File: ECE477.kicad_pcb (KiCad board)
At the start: 2 copper layers, 58 parts, among them IC1 LP3852EMP-3.3_NOPB, IC2 BQ29330DBT, J1 P7805-2000-S, J2 Conn_01x05_Male, J3 Conn_01x05_Male, J4 Conn_01x05_Male, J5 Conn_01x05_Male, J6 Conn_01x05_Male, J7 Conn_01x05_Male, SW1 SW_Push_Dual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

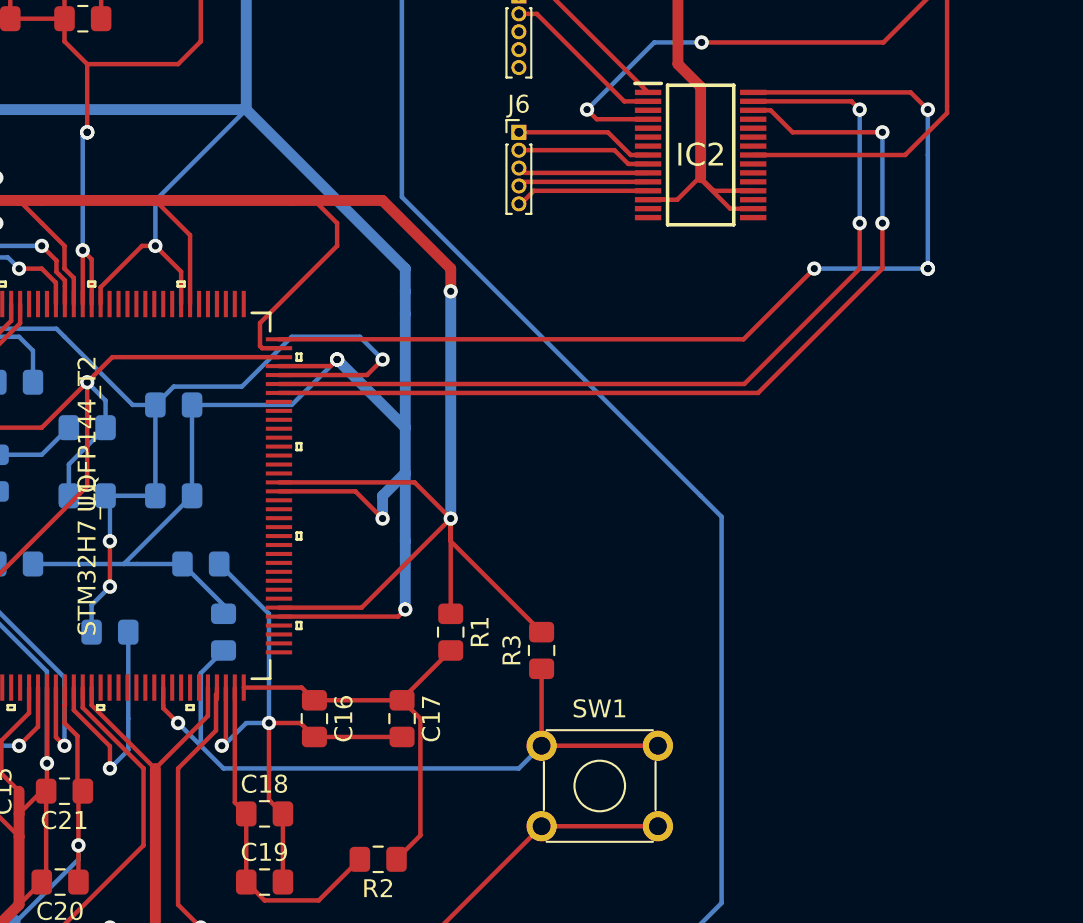
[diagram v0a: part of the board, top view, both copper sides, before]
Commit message: Updated CLK for Bq29330DBT
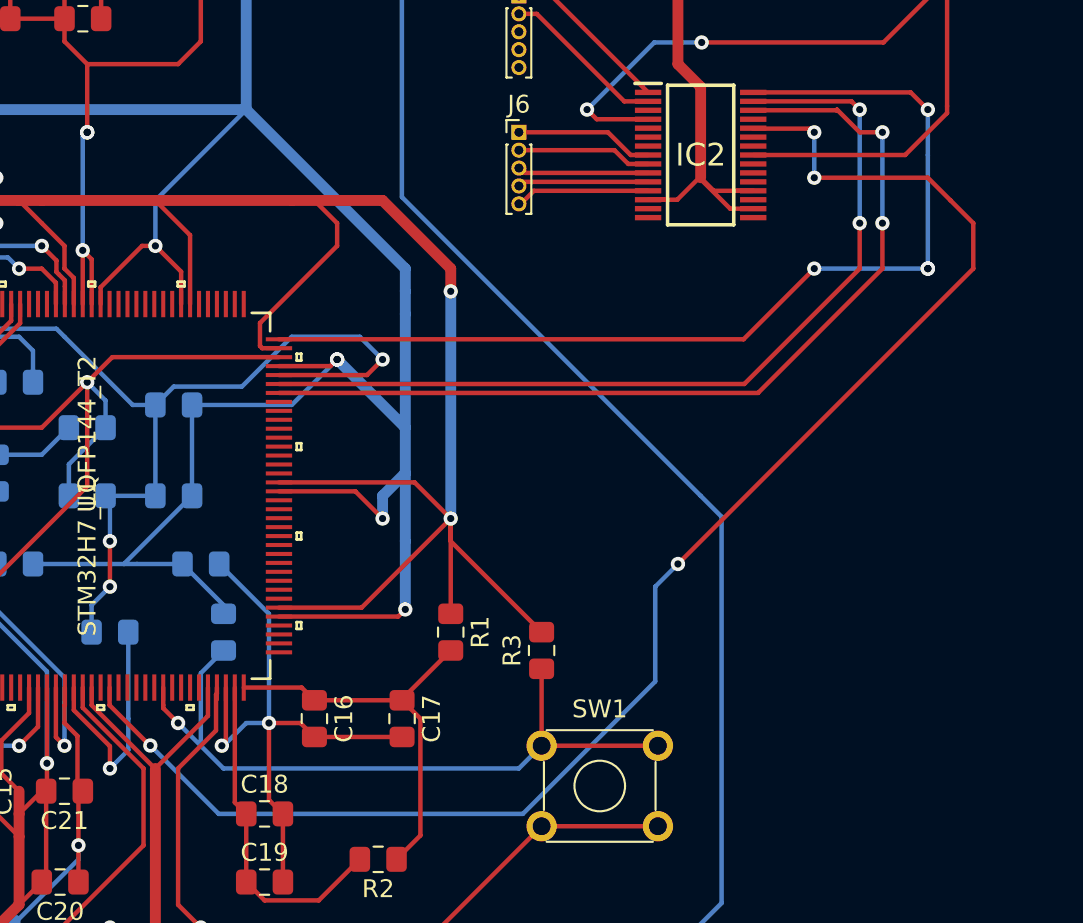
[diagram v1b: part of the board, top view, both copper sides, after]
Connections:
- IC2 pad 26: Net-(IC2-Pad26) -> CLK
- U1 pad 21: Net-(U1-Pad21) -> CLK
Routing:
- net CLK: track 0.00 -> 86.1 mm, vias 0 -> 4

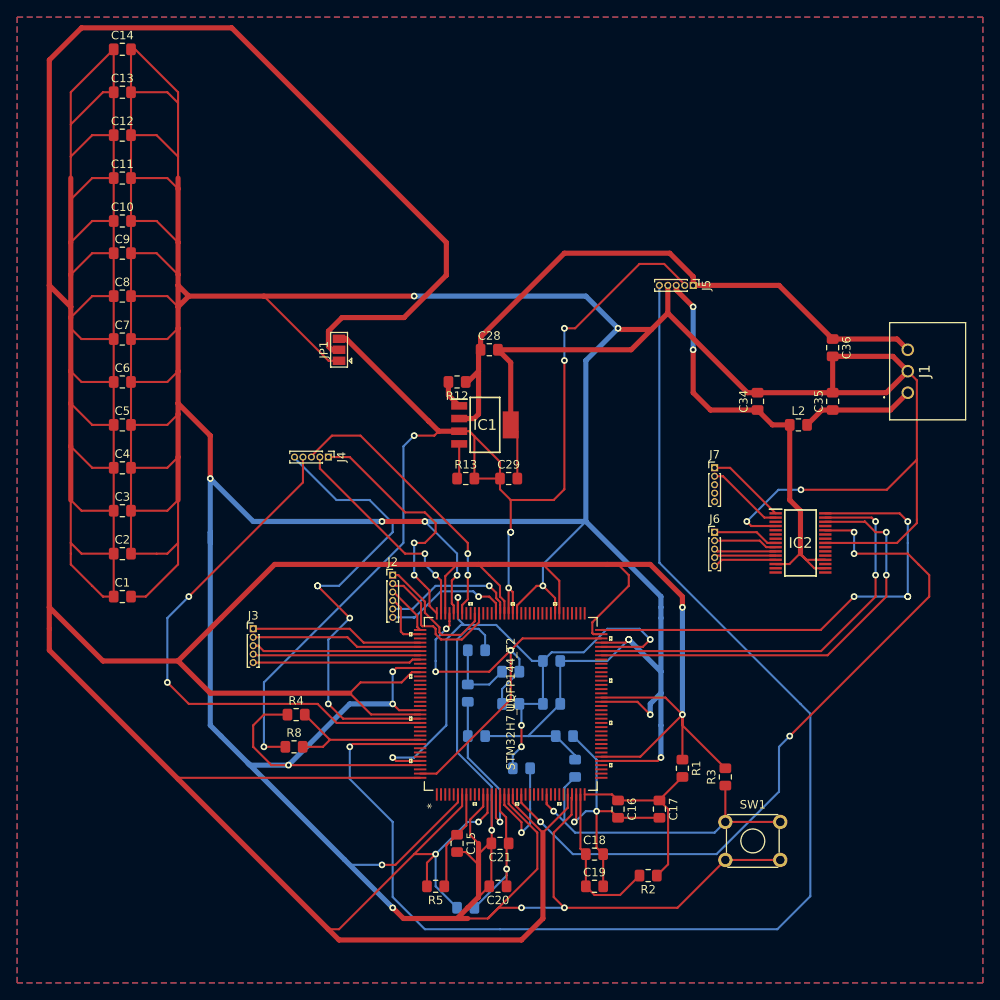
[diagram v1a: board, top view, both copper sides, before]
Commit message: Added mounting Holes
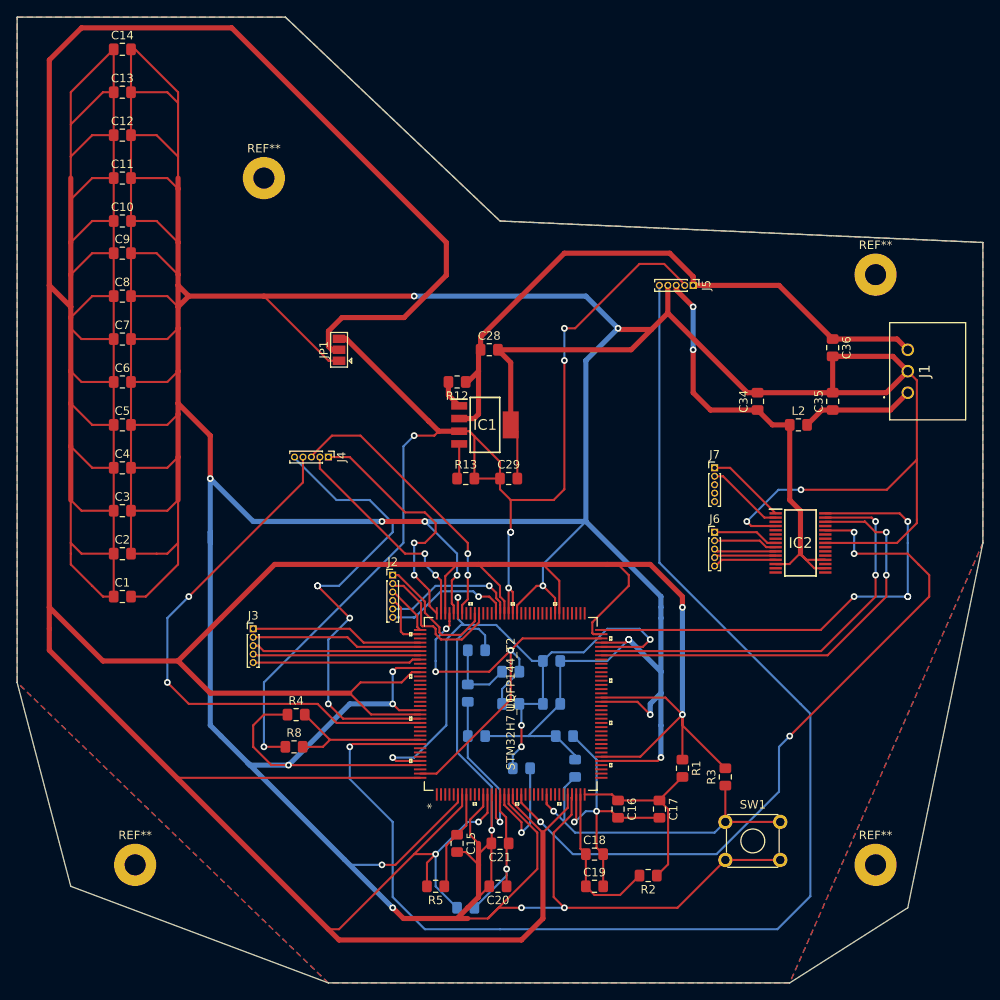
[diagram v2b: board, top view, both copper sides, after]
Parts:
- added REF**: MountingHole_2.5mm_Pad, MountingHole:MountingHole_2.5mm_Pad, F.Cu at (168.9, 44.5)
- added REF**: MountingHole_2.5mm_Pad, MountingHole:MountingHole_2.5mm_Pad, F.Cu at (241.3, 55.9)
- added REF**: MountingHole_2.5mm_Pad, MountingHole:MountingHole_2.5mm_Pad, F.Cu at (153.7, 125.7)
- added REF**: MountingHole_2.5mm_Pad, MountingHole:MountingHole_2.5mm_Pad, F.Cu at (241.3, 125.7)
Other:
- board outline added: 114.3 x 114.3 mm

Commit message: Updates #1 post meeting with TODD
Updated pins and added GNDs for serial communication refreces.
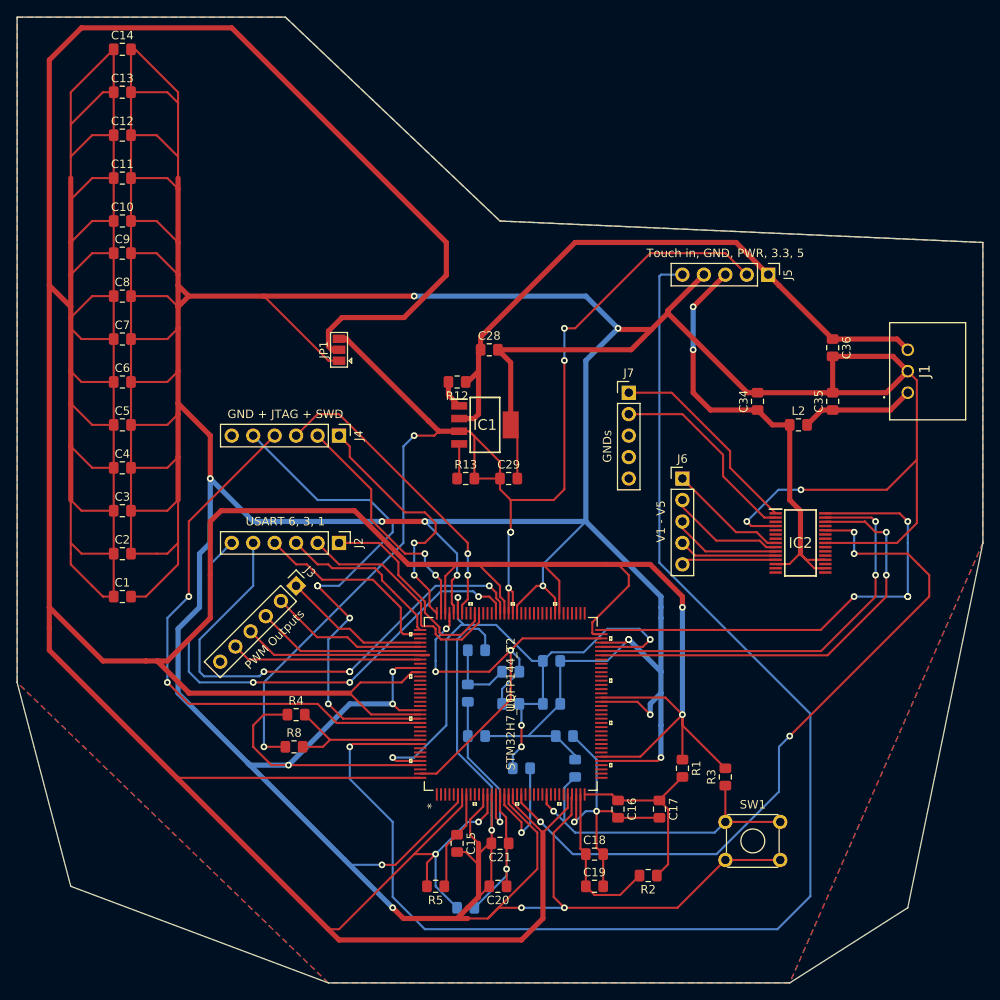
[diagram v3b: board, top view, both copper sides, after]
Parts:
- removed REF** (x4): MountingHole_2.5mm_Pad, MountingHole:MountingHole_2.5mm_Pad
- J2: footprint Connector_PinHeader_1.00mm:PinHeader_1x06_P1.00mm_Vertical -> Connector_PinHeader_2.54mm:PinHeader_1x06_P2.54mm_Vertical
- J3, J4: footprint Connector_PinHeader_1.00mm:PinHeader_1x05_P1.00mm_Vertical -> Connector_PinHeader_2.54mm:PinHeader_1x06_P2.54mm_Vertical
- J5, J6, J7: footprint Connector_PinHeader_1.00mm:PinHeader_1x05_P1.00mm_Vertical -> Connector_PinHeader_2.54mm:PinHeader_1x05_P2.54mm_Vertical
- moved J7 13.5 mm to (212.1, 69.8)
- moved J5 8.98 mm to (228.6, 55.9)
- moved J2 7.41 mm to (177.8, 87.6), turned to 270 degrees
- moved J6 7.41 mm to (218.4, 80.0)
- moved J3 7.18 mm to (172.7, 92.7), turned to 315 degrees
- moved J4 2.84 mm to (177.8, 74.9)
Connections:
- J7 pad 3: Net-(J7-Pad3) -> GND
- J7 pad 4: Net-(J7-Pad4) -> GND
- J7 pad 5: Net-(J7-Pad5) -> GND
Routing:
- net USART6_RX: track 15.3 -> 60.5 mm, vias 1 -> 3
- net USART6_TX: track 16.3 -> 60.6 mm, vias 1 -> 4
- net USART3_RX: track 6.56 -> 23.4 mm
- net CELL-: track 9.45 -> 24.5 mm
- net CELL+: track 9.25 -> 23.9 mm
- net VDD_MCU: track 742.2 -> 756.6 mm
- net USART3_TX: track 5.90 -> 20.1 mm
- net USART1_TX: track 16.7 -> 27.6 mm
- net USART1_RX: track 15.4 -> 24.2 mm
- net 3V3_VDD: track 150.0 -> 157.8 mm
- net V5: track 7.75 -> 14.2 mm
- net V4: track 7.54 -> 13.8 mm
- net JTDO: track 55.7 -> 61.6 mm
- net V3: track 7.72 -> 13.0 mm
- net GND: track 910.1 -> 914.9 mm
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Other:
- board text added: "GND + JTAG + SWD"
- board text added: "GNDs"
- board text added: "PWM Outputs"
- board text added: "Touch in, GND, PWR, 3.3, 5"
- board text added: "USART 6, 3, 1"
- board text added: "V1 - V5"

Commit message: Updated with single cap
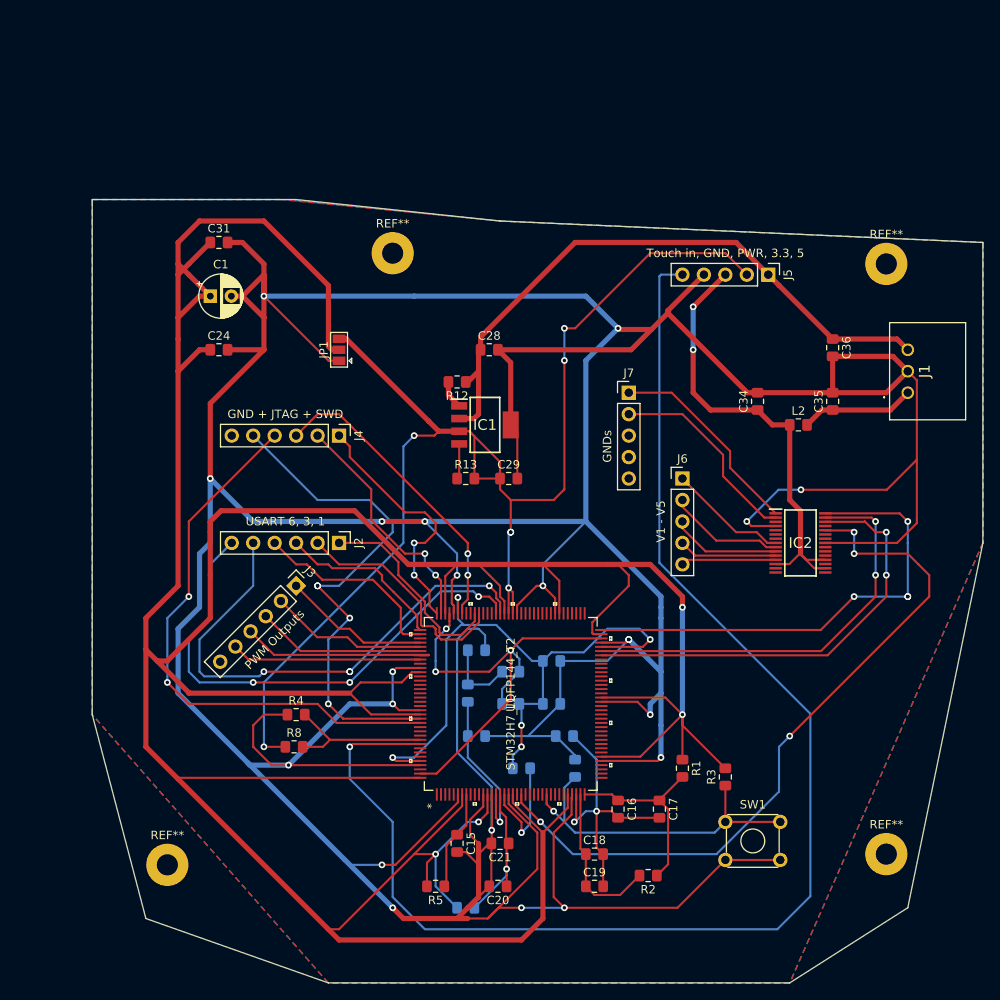
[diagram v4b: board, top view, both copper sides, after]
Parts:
- removed C10, C11, C12, C13, C14, C2, C3, C4, C5, C6, C7, C8, C9: 100nF, Capacitor_SMD:C_0805_2012Metric_Pad1.15x1.40mm_HandSolder
- added C24: 1uF, Capacitor_SMD:C_0805_2012Metric_Pad1.15x1.40mm_HandSolder, F.Cu at (163.6, 64.8)
- added C31: .1uF, Capacitor_SMD:C_0805_2012Metric_Pad1.15x1.40mm_HandSolder, F.Cu at (163.6, 52.1)
- added REF**: MountingHole_2.5mm_Pad, MountingHole:MountingHole_2.5mm_Pad, F.Cu at (242.6, 124.5)
- added REF**: MountingHole_2.5mm_Pad, MountingHole:MountingHole_2.5mm_Pad, F.Cu at (157.5, 125.7)
- added REF**: MountingHole_2.5mm_Pad, MountingHole:MountingHole_2.5mm_Pad, F.Cu at (184.2, 53.3)
- added REF**: MountingHole_2.5mm_Pad, MountingHole:MountingHole_2.5mm_Pad, F.Cu at (242.6, 54.6)
- C1: value 4.7uF -> 10uF; footprint Capacitor_SMD:C_0805_2012Metric_Pad1.15x1.40mm_HandSolder -> Capacitor_THT:CP_Radial_D5.0mm_P2.50mm
- moved C1 37.1 mm to (162.6, 58.4)
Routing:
- net VDD_MCU: track 756.6 -> 476.5 mm
- net GND: track 914.9 -> 735.6 mm
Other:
- board size 114.3 x 114.3 mm -> 105.4 x 92.7 mm

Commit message: Shrunk PCB size
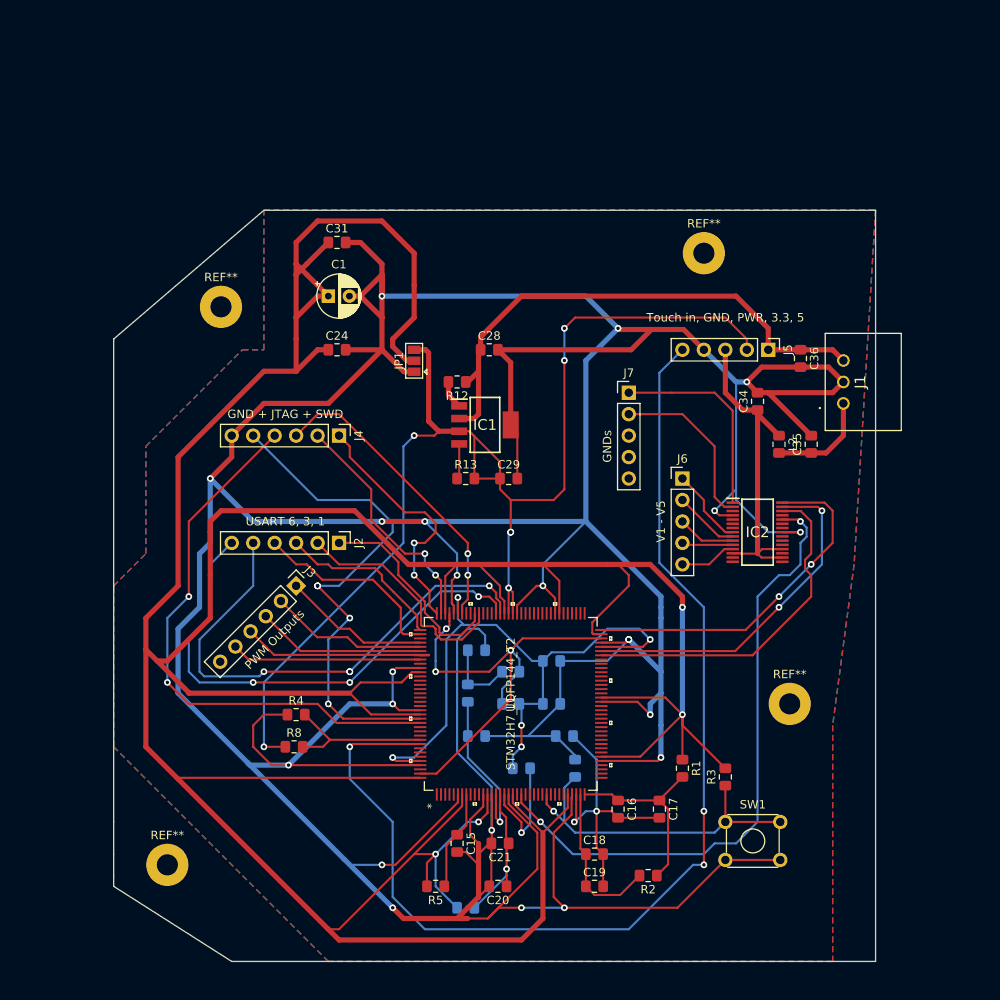
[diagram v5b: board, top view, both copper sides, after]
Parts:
- removed the REF** at (242.6, 124.5)
- removed the REF** at (184.2, 53.3)
- added REF**: MountingHole_2.5mm_Pad, MountingHole:MountingHole_2.5mm_Pad, F.Cu at (231.1, 106.7)
- added REF**: MountingHole_2.5mm_Pad, MountingHole:MountingHole_2.5mm_Pad, F.Cu at (163.8, 59.7)
- moved REF** 21.6 mm to (221.0, 53.3)
- moved C1 14.0 mm to (176.5, 58.4)
- moved C24 14.0 mm to (177.6, 64.8)
- moved C31 14.0 mm to (177.6, 52.1)
- moved JP1 8.98 mm to (186.7, 66.1)
- moved J5 8.89 mm to (228.6, 64.8)
- moved J1 7.73 mm to (237.5, 71.1)
- moved C35 5.68 mm to (233.7, 76.0)
- moved IC2 5.24 mm to (227.3, 86.4)
- moved C36 4.02 mm to (232.4, 65.8)
- moved L2 3.25 mm to (229.9, 76.0), turned to 270 degrees
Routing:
- net GND: track 735.6 -> 689.0 mm, vias 21 -> 22
- net Touch_Input: track 164.6 -> 134.2 mm, vias 1 -> 3
- net PWR_IN: track 57.2 -> 40.6 mm, vias 2 -> 0
- net I2C2_SMBA: track 57.0 -> 41.8 mm, vias 4 -> 2
- net CLK: track 86.1 -> 74.3 mm, vias 4 -> 2
- net 5V: track 74.2 -> 63.4 mm
- net I2C2_SCL: track 52.0 -> 41.1 mm, vias 2 -> 0
- net VDD_MCU: track 476.5 -> 485.8 mm
- net I2C2_SDA: track 50.2 -> 41.6 mm
- net 3V3_VDD: track 157.8 -> 151.3 mm
- net V3: track 13.0 -> 6.89 mm
- net V4: track 13.8 -> 7.74 mm
- net V2: track 11.7 -> 6.05 mm
- net V5: track 14.2 -> 9.33 mm
- net V1: track 11.3 -> 7.47 mm
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- added copper zone on F.Cu, net (none)
- removed copper zone on F.Cu, net GND
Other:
- board size 105.4 x 92.7 mm -> 90.2 x 88.9 mm

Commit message: Added additional outputs on GPIOE
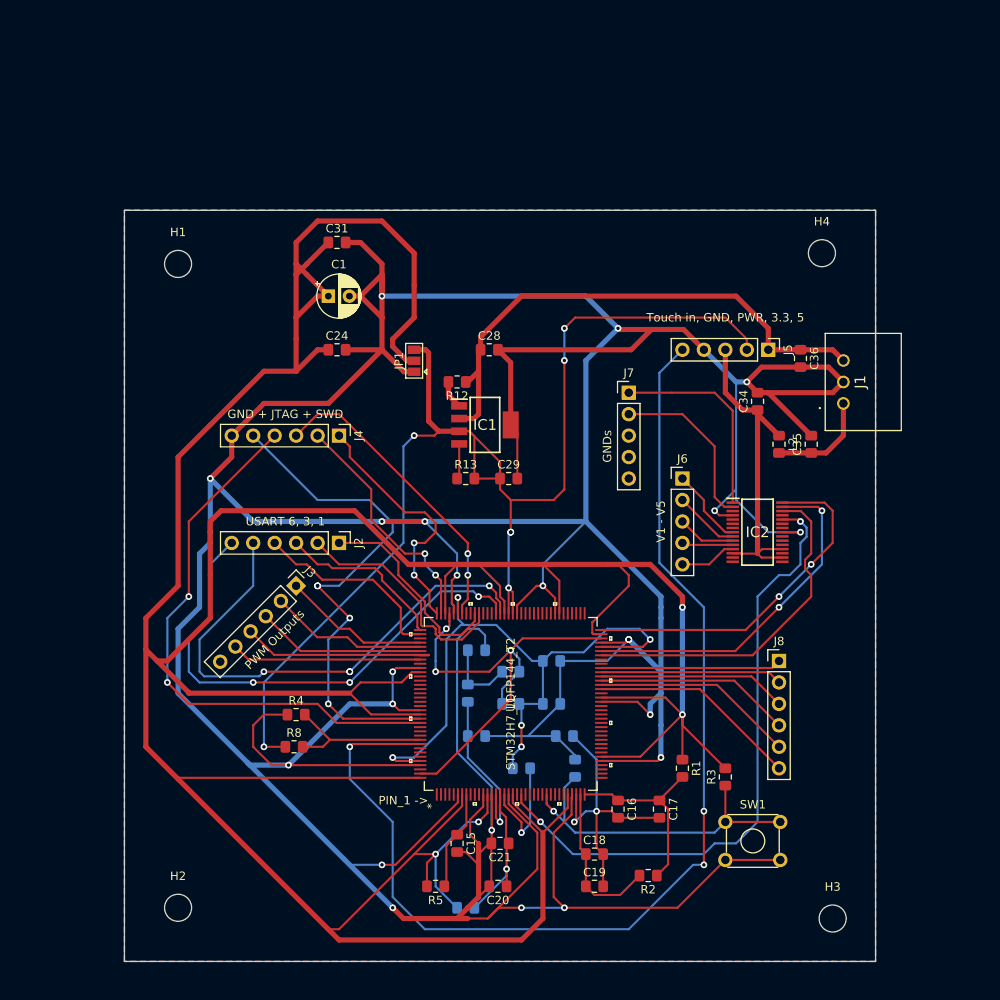
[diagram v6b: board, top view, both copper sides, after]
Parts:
- removed REF** (x4): MountingHole_2.5mm_Pad, MountingHole:MountingHole_2.5mm_Pad
- added H1: MountingHole, MountingHole:MountingHole_3.2mm_M3_ISO14580, F.Cu at (158.8, 54.6)
- added H2: MountingHole, MountingHole:MountingHole_3.2mm_M3_ISO14580, F.Cu at (158.8, 130.8)
- added H3: MountingHole, MountingHole:MountingHole_3.2mm_M3_ISO14580, F.Cu at (236.2, 132.1)
- added H4: MountingHole, MountingHole:MountingHole_3.2mm_M3_ISO14580, F.Cu at (234.9, 53.3)
- added J8: Conn_01x05_Male, Connector_PinHeader_2.54mm:PinHeader_1x06_P2.54mm_Vertical, F.Cu at (229.9, 101.6)
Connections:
- U1 pad 58: Net-(U1-Pad58) -> PIN1
- U1 pad 59: Net-(U1-Pad59) -> PIN2
- U1 pad 60: Net-(U1-Pad60) -> PIN3
- U1 pad 61: Net-(U1-Pad61) -> PIN4
- U1 pad 62: Net-(U1-Pad62) -> PIN5
- U1 pad 63: Net-(U1-Pad63) -> PIN6
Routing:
- net PIN1: track 0.00 -> 24.9 mm
- net PIN2: track 0.00 -> 24.1 mm
- net PIN3: track 0.00 -> 23.2 mm
- net PIN4: track 0.00 -> 22.4 mm
- net PIN5: track 0.00 -> 21.5 mm
- net PIN6: track 0.00 -> 21.4 mm
- added copper zone on F.Cu, net GND
- removed copper zone on F.Cu, net (none)
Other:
- board size 90.2 x 88.9 mm -> 88.9 x 88.9 mm
- board text added: "PIN_1 ->"

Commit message: Updated
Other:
- board text removed: "PIN_1 ->"
